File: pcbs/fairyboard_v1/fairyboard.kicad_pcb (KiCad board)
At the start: 2 copper layers, 305.6 x 118.3 mm, 143 parts

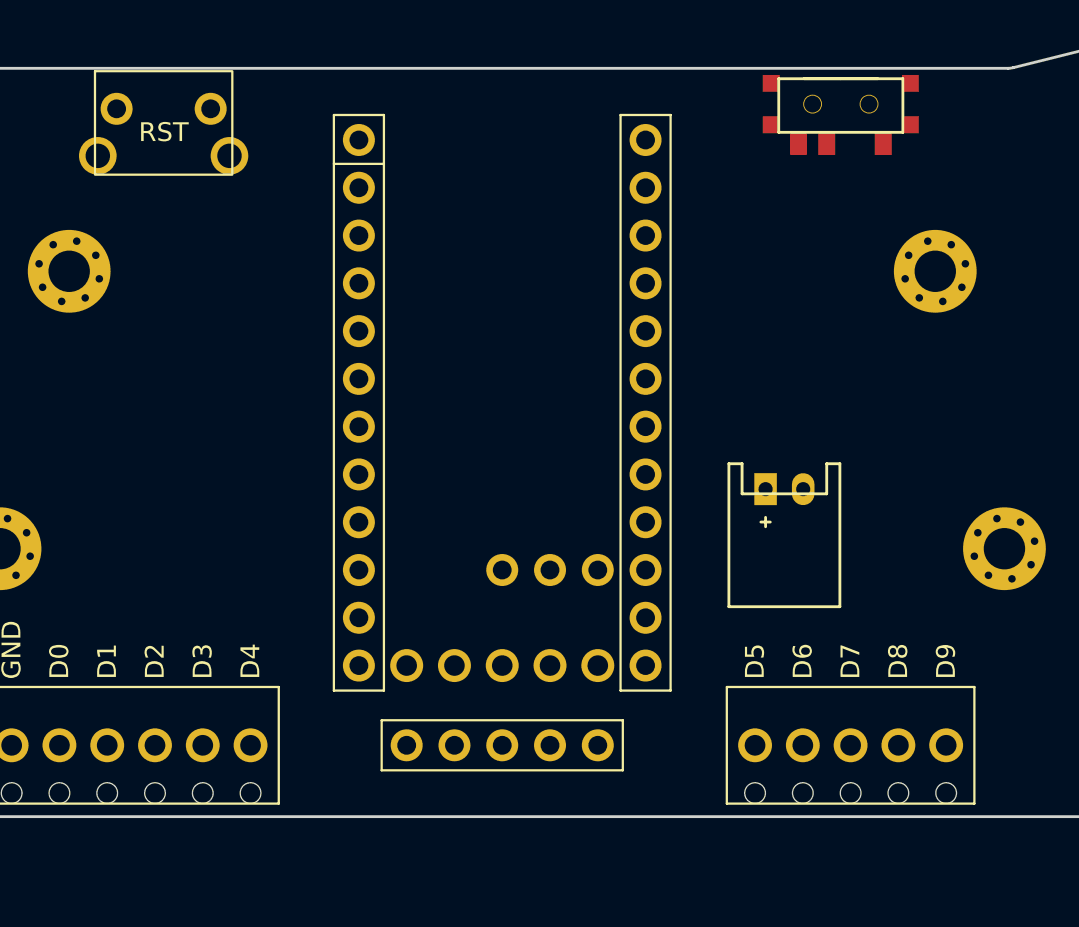
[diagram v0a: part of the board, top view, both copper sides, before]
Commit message: feat: adjustments to top of pcb and silkscreen
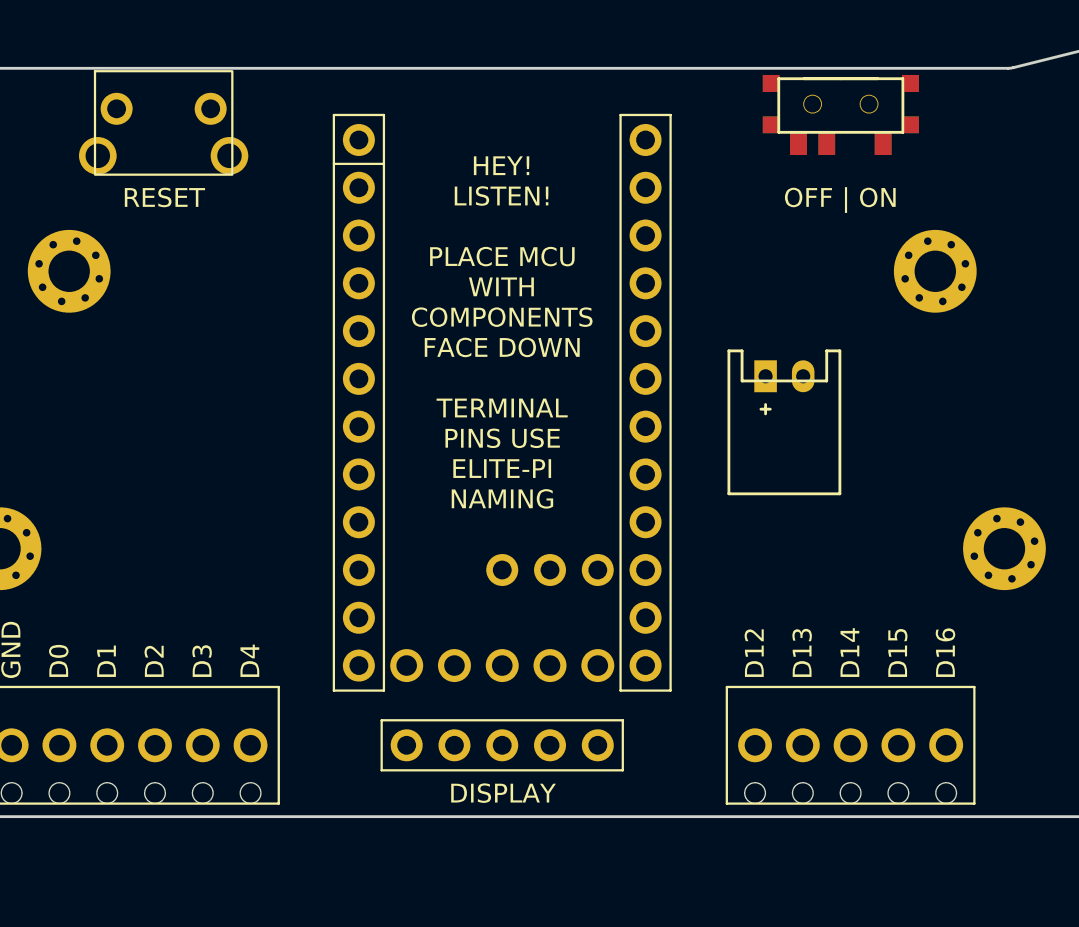
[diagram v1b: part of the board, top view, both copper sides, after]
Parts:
- moved JST1 6.00 mm to (225.5, 130.1)
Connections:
- ? pad 22: D0 -> D1
- ? pad 23: D1 -> D0
- DISP1 pad 5: D1 -> D0
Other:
- board text added: "DISPLAY"
- board text added: "HEY! LISTEN! PLACE MCU WITH COMPONENTS FACE DOWN TERMINAL PINS USE ELITE-PI NAMING"
- board text added: "OFF | ON"
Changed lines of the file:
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@@
 			(layer "Dwgs.User")
 		)
-		(fp_text user "RST"
-			(at 0 0 0)
+		(fp_text user "RESET"
+			(at 0 3.5 0)
 			(layer "F.SilkS")
 			(effects
@@
 			(layers "*.Cu" "*.Mask")
 			(remove_unused_layers no)
-			(net 54 "D1")
+			(net 55 "D0")
 		)
 	)
@@
 		)
 		(pad "" np_thru_hole circle
-			(at 5 -3.749999)
+			(at 5 -3.749998)
 			(size 3 3)
 			(drill 3)
@@
 		)
 		(pad "" np_thru_hole circle
-			(at 5 -3.749999)
+			(at 5 -3.749998)
 			(size 3 3)
 			(drill 3)
@@
 		)
 		(pad "" np_thru_hole circle
-			(at 5 -3.749999)
+			(at 5 -3.749998)
 			(size 3 3)
 			(drill 3)
@@
 		)
 		(pad "" np_thru_hole circle
-			(at 5 -3.749999)
+			(at 5 -3.749998)
 			(size 3 3)
 			(drill 3)
@@
 		)
 		(pad "" np_thru_hole circle
-			(at 5 -3.749999)
+			(at 5 -3.749998)
 			(size 3 3)
 			(drill 3)
@@
 		)
 		(pad "" np_thru_hole circle
-			(at 5 -3.749999)
+			(at 5 -3.749998)
 			(size 3 3)
 			(drill 3)
@@
 		)
 		(pad "" np_thru_hole circle
-			(at 5 -3.749999)
+			(at 5 -3.749998)
 			(size 3 3)
 			(drill 3)
@@
 		)
 		(pad "" np_thru_hole circle
-			(at 5 -3.749999)
+			(at 5 -3.749998)
 			(size 3 3)
 			(drill 3)
@@
 		)
 		(pad "" np_thru_hole circle
-			(at 5 -3.749999)
+			(at 5 -3.749998)
 			(size 3 3)
 			(drill 3)
@@
 		)
 		(pad "" np_thru_hole circle
-			(at 5 -3.749999)
+			(at 5 -3.749998)
 			(size 3 3)
 			(drill 3)
@@
 		)
 		(pad "" np_thru_hole circle
-			(at 5 -3.749999)
+			(at 5 -3.749998)
 			(size 3 3)
 			(drill 3)
@@
 		)
 		(pad "" np_thru_hole circle
-			(at 5 -3.749999)
+			(at 5 -3.749998)
 			(size 3 3)
 			(drill 3)
@@
 			(layers "*.Cu" "*.Mask")
 			(remove_unused_layers no)
-			(net 55 "D0")
+			(net 54 "D1")
 		)
 		(pad "23" thru_hole oval
@@
 			(layers "*.Cu" "*.Mask")
 			(remove_unused_layers no)
-			(net 54 "D1")
+			(net 55 "D0")
 		)
 		(pad "24" thru_hole oval
@@
 	(footprint "JST_PH_S2B-PH-K_02x2.00mm_Angled"
 		(layer "F.Cu")
-		(at 225.458897 136.125906)
+		(at 225.458897 130.125906)
 		(descr "JST PH series connector, S2B-PH-K, side entry type, through hole, Datasheet: http://www.jst-mfg.com/product/pdf/eng/ePH.pdf")
 		(tags "connector jst ph")
@@
 		)
 		(pad "" np_thru_hole circle
-			(at 5 -3.749999)
+			(at 5 -3.749998)
 			(size 3 3)
 			(drill 3)
@@
 		)
 		(pad "" np_thru_hole circle
-			(at 5 -3.749999)
+			(at 5 -3.749998)
 			(size 3 3)
 			(drill 3)
@@
 		)
 		(pad "" np_thru_hole circle
-			(at 5 -3.749999)
+			(at 5 -3.749998)
 			(size 3 3)
 			(drill 3)
@@
 		)
 		(pad "" np_thru_hole circle
-			(at 5 -3.749999)
+			(at 5 -3.749998)
 			(size 3 3)
 			(drill 3)
@@
 			(layer "F.CrtYd")
 		)
-		(fp_text user "D7"
+		(fp_text user "D14"
 			(at -1.27 13.2 90)
 			(layer "F.SilkS")
@@
 			)
 		)
-		(fp_text user "D6"
+		(fp_text user "D13"
 			(at -3.81 13.2 90)
 			(layer "F.SilkS")
@@
 			)
 		)
-		(fp_text user "D5"
+		(fp_text user "D12"
 			(at -6.35 13.2 90)
 			(layer "F.SilkS")
@@
 			)
 		)
-		(fp_text user "D8"
+		(fp_text user "D15"
 			(at 1.27 13.2 90)
 			(layer "F.SilkS")
@@
 			)
 		)
-		(fp_text user "D9"
+		(fp_text user "D16"
 			(at 3.81 13.2 90)
 			(layer "F.SilkS")
@@
 		)
 		(pad "" np_thru_hole circle
-			(at 5 -3.749999)
+			(at 5 -3.749998)
 			(size 3 3)
 			(drill 3)
@@
 		)
 		(pad "" np_thru_hole circle
-			(at 5 -3.749999)
+			(at 5 -3.749998)
 			(size 3 3)
 			(drill 3)
@@
 		(layer "Edge.Cuts")
 	)
+	(gr_text "HEY!\nLISTEN!\n\nPLACE MCU\nWITH\nCOMPONENTS\nFACE DOWN\n\nTERMINAL\nPINS USE\nELITE-PI\nNAMING"
+		(at 210.458897 137.264906 0)
+		(layer "F.SilkS")
+		(effects
+			(font
+				(size 1 1)
+				(thickness 0.15)
+			)
+			(justify bottom)
+		)
+	)
+	(gr_text "DISPLAY"
+		(at 210.458897 152.323906 0)
+		(layer "F.SilkS")
+		(effects
+			(font
+				(size 1 1)
+				(thickness 0.15)
+			)
+		)
+	)
+	(gr_text "OFF | ON"
+		(at 228.458897 120.657355 0)
+		(layer "F.SilkS")
+		(effects
+			(font
+				(size 1 1)
+				(thickness 0.15)
+			)
+		)
+	)
 )

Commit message: feat: route middle of pcb
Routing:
- net D0: track 0.00 -> 64.2 mm, vias 0 -> 1
- net VCC: track 0.00 -> 56.0 mm
- net RAW: track 0.00 -> 41.9 mm
- net D2: track 0.00 -> 41.7 mm
- net D3: track 0.00 -> 38.8 mm, vias 0 -> 2
- net D9: track 0.00 -> 31.8 mm
- net D4: track 0.00 -> 28.8 mm
- net D8: track 0.00 -> 26.4 mm, vias 0 -> 1
- net D7: track 0.00 -> 25.4 mm
- net D6: track 0.00 -> 20.7 mm, vias 0 -> 1
- net RST: track 0.00 -> 15.7 mm
- net D5: track 0.00 -> 15.2 mm
- net B+: track 0.00 -> 13.7 mm
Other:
- rule pad_to_mask_clearance: 0.05 -> 0

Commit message: feat: first routing pass
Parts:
- moved D28 1.94 mm to (315.2, 113.9)
- moved D10 1.94 mm to (136.4, 137.5)
- moved S31 1.94 mm to (288.3, 113.7)
- moved S71 1.94 mm to (288.3, 113.7)
- moved JST1 1.94 mm to (226.7, 131.6)
- moved S33 1.94 mm to (275.7, 141.6)
- moved S73 1.94 mm to (275.7, 141.6)
- moved S45 1.94 mm to (94.9, 117.6)
- moved S5 1.94 mm to (94.9, 117.6)
- moved _7 1.94 mm to (300.3, 122.5)
- moved S37 1.94 mm to (253.5, 131.1)
- moved S77 1.94 mm to (253.5, 131.1)
- moved D6 1.94 mm to (112.6, 154.2)
- moved D8 1.94 mm to (121.8, 117.3)
- moved _17 1.94 mm to (234.7, 126.0)
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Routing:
- net COL1: track 0.00 -> 423.1 mm, vias 0 -> 1
- net COL2: track 0.00 -> 384.7 mm, vias 0 -> 1
- net COL4: track 0.00 -> 351.8 mm, vias 0 -> 3
- net COL3: track 0.00 -> 342.7 mm, vias 0 -> 3
- net COL5: track 0.00 -> 295.4 mm, vias 0 -> 1
- net COL6: track 0.00 -> 262.6 mm, vias 0 -> 4
- net ROW4: track 0.00 -> 229.6 mm, vias 0 -> 6
- net ROW7: track 0.00 -> 228.5 mm, vias 0 -> 1
- net ROW5: track 0.00 -> 217.7 mm, vias 0 -> 17
- net ROW3: track 0.00 -> 206.2 mm, vias 0 -> 12
- net ROW6: track 0.00 -> 204.0 mm, vias 0 -> 11
- net ROW2: track 0.00 -> 171.7 mm, vias 0 -> 12
- net ROW1: track 0.00 -> 139.7 mm, vias 0 -> 6
- net D1: track 0.00 -> 50.4 mm, vias 0 -> 5
- net RAW: track 41.9 -> 72.6 mm, vias 0 -> 2
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
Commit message: feat: fully connected pcb
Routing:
- net ROW5: track 217.7 -> 215.1 mm
- net COL4: track 351.8 -> 349.4 mm
- net ROW7: track 228.5 -> 226.3 mm
- net ROW6: track 204.0 -> 201.7 mm
- net COL5: track 295.4 -> 293.2 mm
- net COL3: track 342.7 -> 340.5 mm
- net COL2: track 384.7 -> 382.5 mm
- net COL6: track 262.6 -> 260.8 mm
- net ROW3: track 206.2 -> 204.4 mm
- net COL1: track 423.1 -> 421.4 mm
- net ROW4: track 229.6 -> 228.3 mm
- net VCC: track 56.0 -> 57.0 mm
- net ROW1: track 139.7 -> 138.7 mm
- net D0: track 65.5 -> 64.8 mm
- net GND: vias 0 -> 248
- added copper zone on B.Cu, net GND
- added copper zone on F.Cu, net GND

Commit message: feat: fairyboard branding
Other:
- board text added: "fairyboard"
- board text added: "v1.0"

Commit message: feat: restive.engines branding
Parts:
- added G***: LOGO, LOGO, F.Cu at (250.1, 117.3)
